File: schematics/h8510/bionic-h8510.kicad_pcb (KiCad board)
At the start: 4 copper layers, 25.4 x 68.6 mm, 16 parts, among them J1 Bionic-P135, J2 Bionic-P245, U1 HD6415108F, U2 11AA010-I/TT, U3 74HCS153, U4 74HCS153, U5 74AHCT157

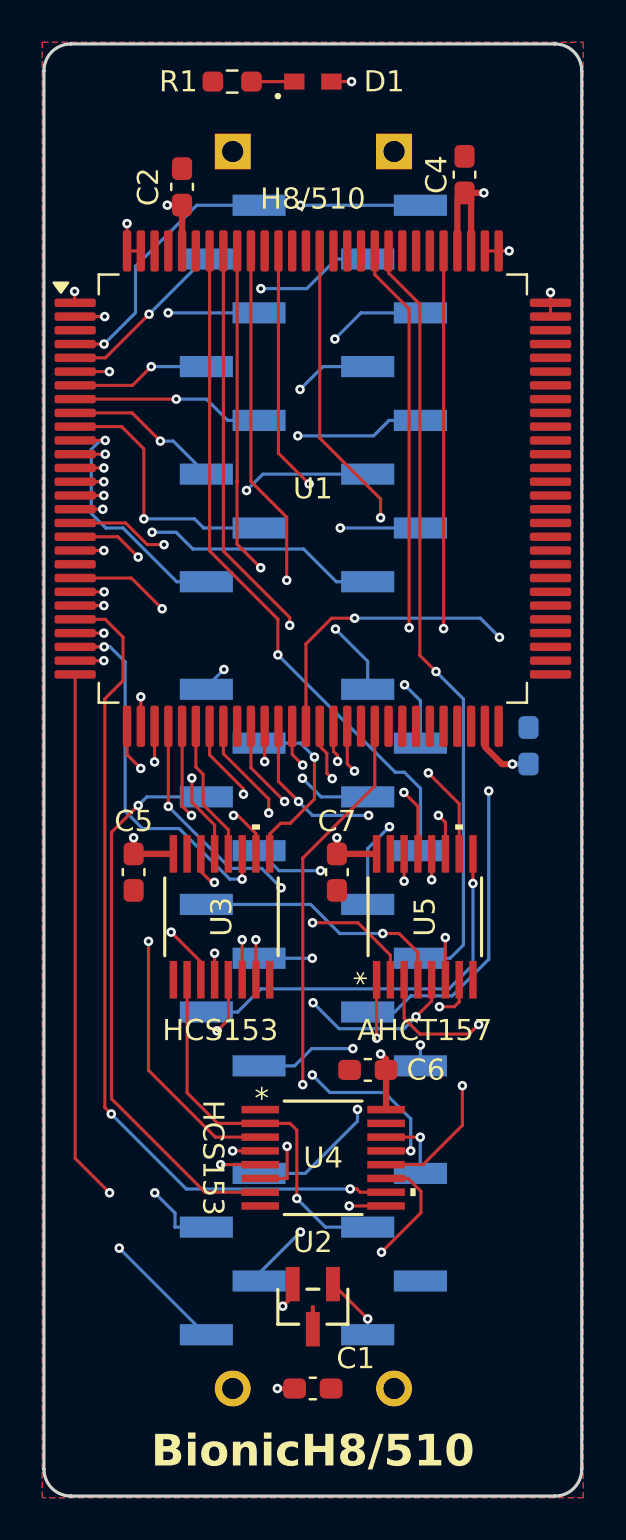
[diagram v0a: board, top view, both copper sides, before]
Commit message: [h8510] [h8536] End the boards' tracks on their pad centres
Re-run the track straightener with the pad-centre fixes (#184) and
regenerate the Gerbers.
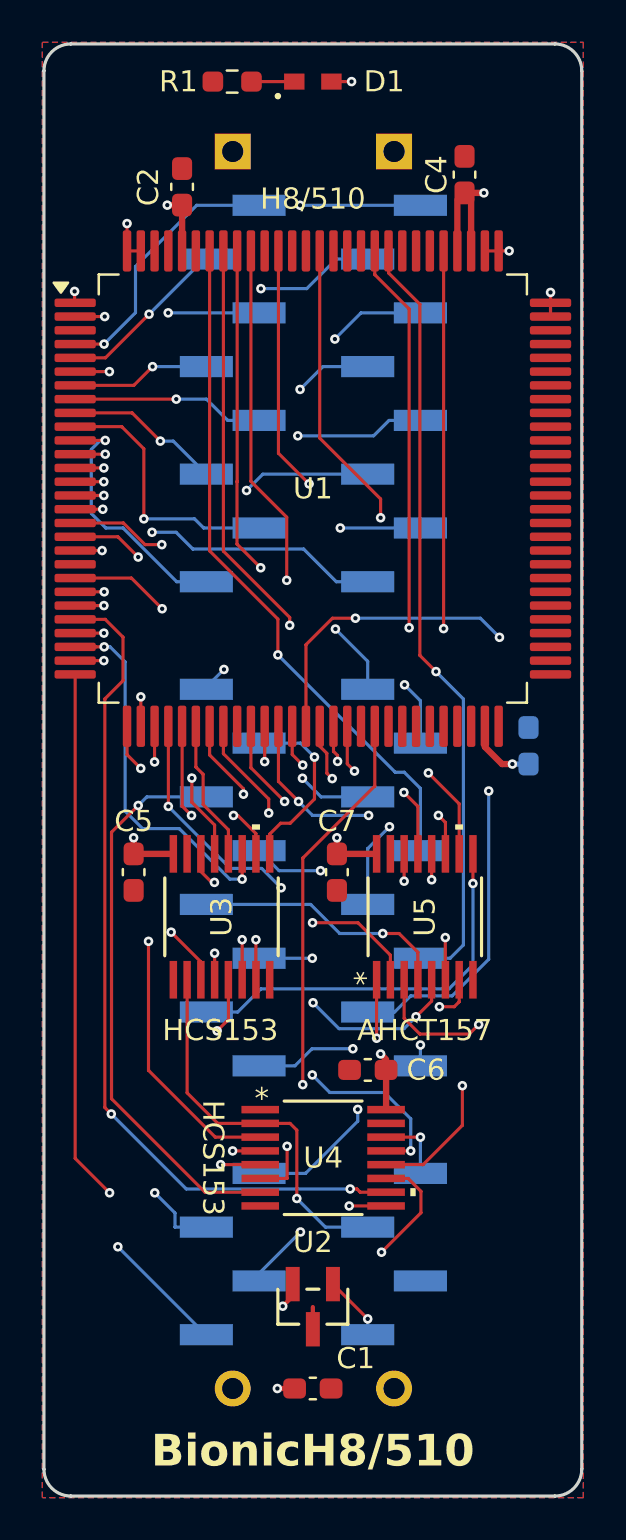
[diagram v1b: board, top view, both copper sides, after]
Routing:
- net A21: track 14.9 -> 15.8 mm
- net ASEL0: track 25.1 -> 25.9 mm
- net A8: track 12.6 -> 13.4 mm
- net A5: track 17.0 -> 17.8 mm
- net A10: track 22.2 -> 23.0 mm
- net VCC: track 26.2 -> 26.7 mm
